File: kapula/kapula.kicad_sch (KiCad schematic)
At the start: 160 parts, among them J1 Conn_02x10_Odd_Even, J12 U.FL, J13 U.FL, J3 U.FL, J4 Conn_ARM_JTAG_SWD_10, J5 U.FL, J9 U.FL, Q1 AO3401A, Q1 BSS84, Q2 AO3401A, Q3 AO3400A, Q5 AO3400A, Q6 AO3400A, T1 BW21S7511A01TF, T2 BW21S7511A01TF, T3 BW21S7511A01TF, T4 BW21S7511A01TF, U1 XC6206P332MR, U2 TP4054, U3 DW01+G, U5 EFR32FG14P233F256GM48-B, U6 XA213-G4J, X1 DSB221SDN, Y1 32768 Hz

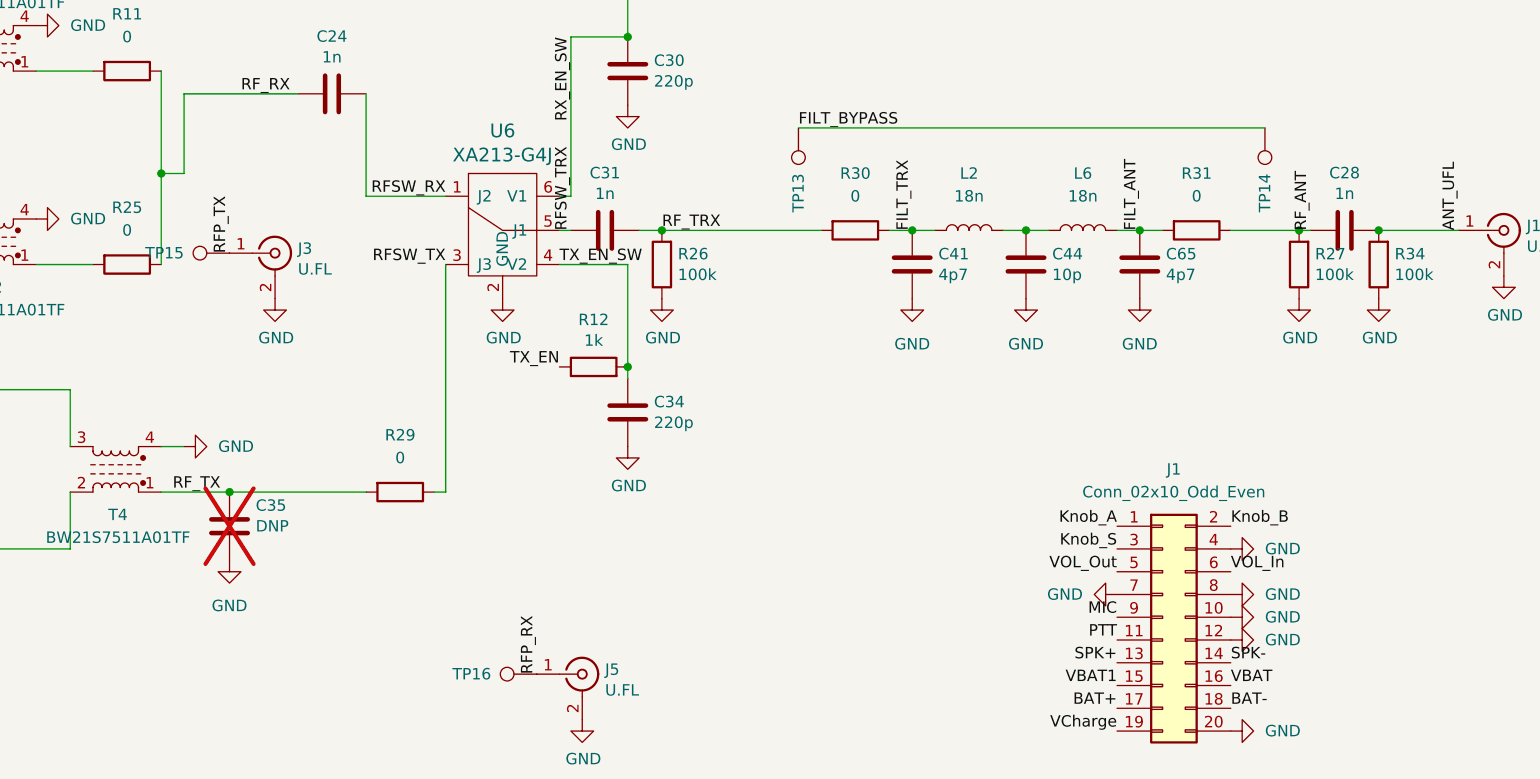
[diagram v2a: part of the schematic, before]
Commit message: Length match balanced TX line
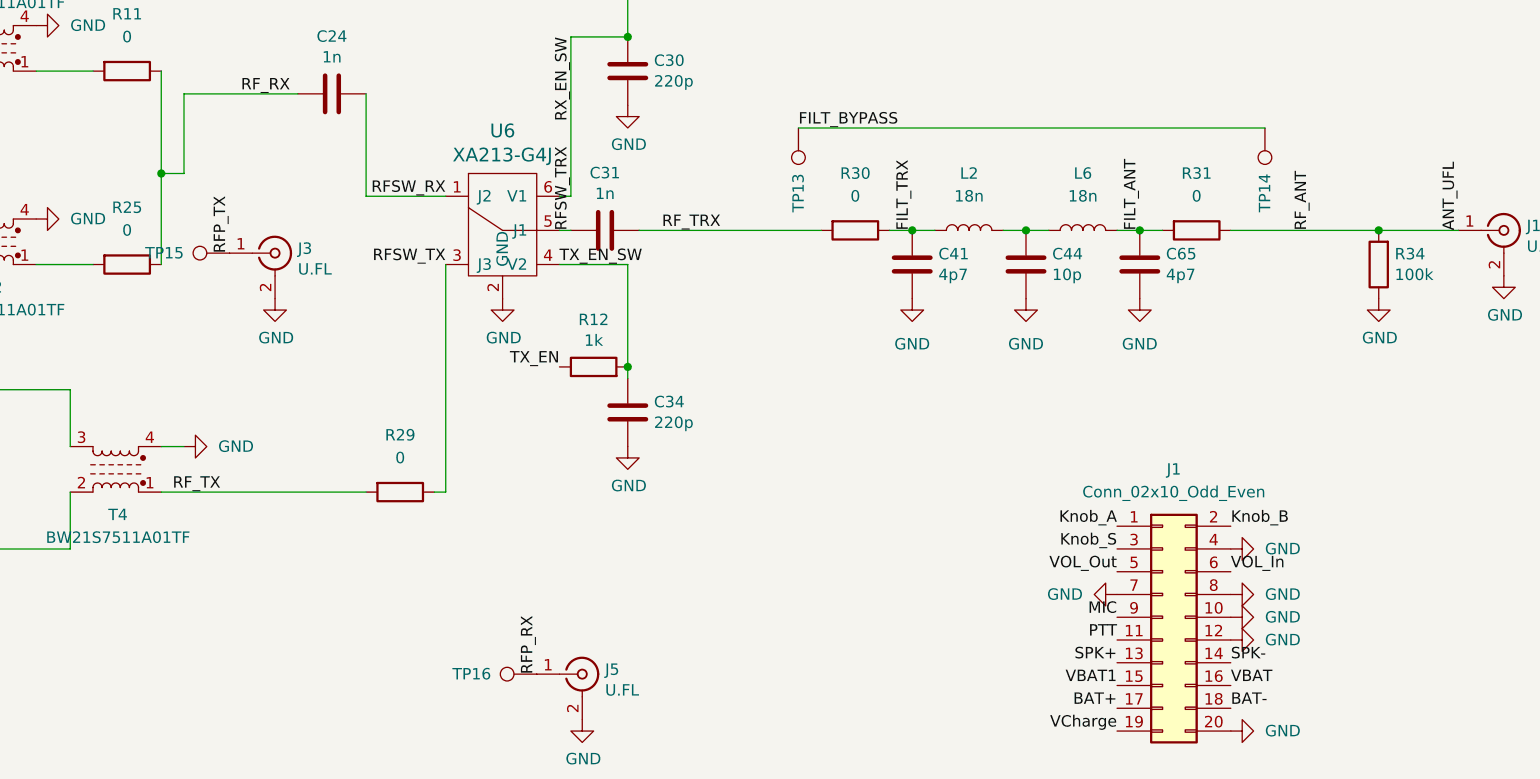
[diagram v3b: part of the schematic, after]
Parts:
- removed C28: 1n, Capacitor_SMD:C_0402_1005Metric, symbol Device:C
- removed C35: DNP, kapula:C_0402_to_0603_HandSolder, symbol Device:C
- removed R26, R27: 100k, Resistor_SMD:R_0402_1005Metric, symbol Device:R
- L10, L7: footprint Inductor_SMD:L_0402_1005Metric -> kapula:L_0402_to_0603_HandSolder
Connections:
- net RF_ANT is gone; now on net ANT_UFL: R31.1
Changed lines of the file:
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@@
   (junction (at 214.63 26.67) (diameter 0) (color 0 0 0 0)
   )
-  (junction (at 391.16 142.24) (diameter 0) (color 0 0 0 0)
-  )
   (junction (at 350.52 57.15) (diameter 0) (color 0 0 0 0)
   )
@@
   (junction (at 171.45 46.99) (diameter 0) (color 0 0 0 0)
   )
-  (junction (at 311.15 142.24) (diameter 0) (color 0 0 0 0)
-  )
   (junction (at 82.55 203.2) (diameter 0) (color 0 0 0 0)
   )
@@
   (junction (at 157.48 39.37) (diameter 0) (color 0 0 0 0)
   )
-  (junction (at 382.27 142.24) (diameter 0) (color 0 0 0 0)
-  )
   (junction (at 173.99 189.23) (diameter 0) (color 0 0 0 0)
   )
@@
   (junction (at 231.14 132.08) (diameter 0) (color 0 0 0 0)
   )
+  (junction (at 391.16 142.24) (diameter 0) (color 0 0 0 0)
+  )
   (junction (at 185.42 137.16) (diameter 0) (color 0 0 0 0)
   )
@@
   (junction (at 156.21 82.55) (diameter 0) (color 0 0 0 0)
   )
-  (junction (at 262.89 171.45) (diameter 0) (color 0 0 0 0)
-  )
   (junction (at 66.04 26.67) (diameter 0) (color 0 0 0 0)
   )
@@
     (stroke (width 0) (type default))
   )
-  (wire (pts (xy 311.15 142.24) (xy 328.93 142.24))
-    (stroke (width 0) (type default))
-  )
-  (wire (pts (xy 262.89 171.45) (xy 278.13 171.45))
+  (wire (pts (xy 308.61 142.24) (xy 328.93 142.24))
     (stroke (width 0) (type default))
   )
@@
     (stroke (width 0) (type default))
   )
-  (wire (pts (xy 382.27 142.24) (xy 383.54 142.24))
+  (wire (pts (xy 374.65 142.24) (xy 391.16 142.24))
     (stroke (width 0) (type default))
   )
@@
     (stroke (width 0) (type default))
   )
-  (wire (pts (xy 374.65 142.24) (xy 382.27 142.24))
-    (stroke (width 0) (type default))
-  )
   (wire (pts (xy 220.98 119.38) (xy 231.14 119.38))
     (stroke (width 0) (type default))
@@
     (stroke (width 0) (type default))
   )
-  (wire (pts (xy 308.61 142.24) (xy 311.15 142.24))
-    (stroke (width 0) (type default))
-  )
   (wire (pts (xy 176.53 85.09) (xy 176.53 124.46))
     (stroke (width 0) (type default))
@@
     (stroke (width 0) (type default))
   )
-  (wire (pts (xy 262.89 171.45) (xy 255.27 171.45))
+  (wire (pts (xy 255.27 171.45) (xy 278.13 171.45))
     (stroke (width 0) (type default))
   )
@@
     )
   )
-  (symbol (lib_id "Device:R") (at 311.15 146.05 180) (unit 1)
-    (in_bom yes) (on_board yes) (dnp no)
-    (property "Reference" "R26" (at 312.928 144.8816 0)
-      (effects (font (size 1.27 1.27)) (justify right))
-    )
-    (property "Value" "100k" (at 312.928 147.193 0)
-      (effects (font (size 1.27 1.27)) (justify right))
-    )
-    (property "Footprint" "Resistor_SMD:R_0402_1005Metric" (at 312.928 146.05 90)
-      (effects (font (size 1.27 1.27)) hide)
-    )
-    (property "Datasheet" "" (at 311.15 146.05 0)
-      (effects (font (size 1.27 1.27)) hide)
-    )
-    (property "LCSC" "" (at 311.15 146.05 0)
-      (effects (font (size 1.27 1.27)) hide)
-    )
-    (pin "1")
-    (pin "2")
-    (instances
-      (project "kapula"
-        (path "/f2315993-072e-45c9-8c85-e79c6d40aba4"
-          (reference "R26") (unit 1)
-        )
-      )
-    )
-  )
   (symbol (lib_id "power:GND") (at 241.3 140.97 90) (unit 1)
     (in_bom yes) (on_board yes) (dnp no) (fields_autoplaced)
@@
     )
   )
-  (symbol (lib_id "Device:R") (at 382.27 146.05 180) (unit 1)
-    (in_bom yes) (on_board yes) (dnp no)
-    (property "Reference" "R27" (at 384.048 144.8816 0)
-      (effects (font (size 1.27 1.27)) (justify right))
-    )
-    (property "Value" "100k" (at 384.048 147.193 0)
-      (effects (font (size 1.27 1.27)) (justify right))
-    )
-    (property "Footprint" "Resistor_SMD:R_0402_1005Metric" (at 384.048 146.05 90)
-      (effects (font (size 1.27 1.27)) hide)
-    )
-    (property "Datasheet" "" (at 382.27 146.05 0)
-      (effects (font (size 1.27 1.27)) hide)
-    )
-    (property "LCSC" "" (at 382.27 146.05 0)
-      (effects (font (size 1.27 1.27)) hide)
-    )
-    (pin "1")
-    (pin "2")
-    (instances
-      (project "kapula"
-        (path "/f2315993-072e-45c9-8c85-e79c6d40aba4"
-          (reference "R27") (unit 1)
-        )
-      )
-    )
-  )
   (symbol (lib_id "Device:C") (at 215.9 265.43 0) (unit 1)
     (in_bom yes) (on_board yes) (dnp no)
@@
     )
   )
-  (symbol (lib_id "Device:C") (at 262.89 175.26 0) (unit 1)
-    (in_bom no) (on_board yes) (dnp yes)
-    (property "Reference" "C35" (at 265.811 172.9486 0)
-      (effects (font (size 1.27 1.27)) (justify left))
-    )
-    (property "Value" "DNP" (at 265.811 175.26 0)
-      (effects (font (size 1.27 1.27)) (justify left))
-    )
-    (property "Footprint" "kapula:C_0402_to_0603_HandSolder" (at 263.8552 179.07 0)
-      (effects (font (size 1.27 1.27)) hide)
-    )
-    (property "Datasheet" "" (at 262.89 175.26 0)
-      (effects (font (size 1.27 1.27)) hide)
-    )
-    (pin "1")
-    (pin "2")
-    (instances
-      (project "kapula"
-        (path "/f2315993-072e-45c9-8c85-e79c6d40aba4"
-          (reference "C35") (unit 1)
-        )
-      )
-    )
-  )
   (symbol (lib_id "Transistor_FET:BSS84") (at 386.08 -19.05 270) (mirror x) (unit 1)
     (in_bom yes) (on_board yes) (dnp no)
@@
     )
   )
-  (symbol (lib_id "power:GND") (at 262.89 179.07 0) (unit 1)
-    (in_bom yes) (on_board yes) (dnp no) (fields_autoplaced)
-    (property "Reference" "#PWR0112" (at 262.89 185.42 0)
-      (effects (font (size 1.27 1.27)) hide)
-    )
-    (property "Value" "GND" (at 262.89 184.15 0)
-      (effects (font (size 1.27 1.27)))
-    )
-    (property "Footprint" "" (at 262.89 179.07 0)
-      (effects (font (size 1.27 1.27)) hide)
-    )
-    (property "Datasheet" "" (at 262.89 179.07 0)
-      (effects (font (size 1.27 1.27)) hide)
-    )
-    (pin "1")
-    (instances
-      (project "kapula"
-        (path "/f2315993-072e-45c9-8c85-e79c6d40aba4"
-          (reference "#PWR0112") (unit 1)
-        )
-      )
-    )
-  )
   (symbol (lib_id "power:GND") (at 373.38 218.44 0) (unit 1)
     (in_bom yes) (on_board yes) (dnp no)
@@
       (effects (font (size 1.27 1.27)))
     )
-    (property "Footprint" "Inductor_SMD:L_0402_1005Metric" (at 195.58 177.8 0)
+    (property "Footprint" "kapula:L_0402_to_0603_HandSolder" (at 195.58 177.8 0)
       (effects (font (size 1.27 1.27)) hide)
     )
@@
     )
   )
-  (symbol (lib_id "power:GND") (at 382.27 149.86 0) (unit 1)
-    (in_bom yes) (on_board yes) (dnp no)
-    (property "Reference" "#PWR0110" (at 382.27 156.21 0)
-      (effects (font (size 1.27 1.27)) hide)
-    )
-    (property "Value" "GND" (at 382.397 154.2542 0)
-      (effects (font (size 1.27 1.27)))
-    )
-    (property "Footprint" "" (at 382.27 149.86 0)
-      (effects (font (size 1.27 1.27)) hide)
-    )
-    (property "Datasheet" "" (at 382.27 149.86 0)
-      (effects (font (size 1.27 1.27)) hide)
-    )
-    (pin "1")
-    (instances
-      (project "kapula"
-        (path "/f2315993-072e-45c9-8c85-e79c6d40aba4"
-          (reference "#PWR0110") (unit 1)
-        )
-      )
-    )
-  )
   (symbol (lib_id "Device:R") (at 377.19 -17.78 180) (unit 1)
     (in_bom yes) (on_board yes) (dnp no)
@@
     )
   )
-  (symbol (lib_id "Device:C") (at 387.35 142.24 270) (unit 1)
-    (in_bom yes) (on_board yes) (dnp no)
-    (property "Reference" "C28" (at 387.35 135.8392 90)
-      (effects (font (size 1.27 1.27)))
-    )
-    (property "Value" "1n" (at 387.35 138.1506 90)
-      (effects (font (size 1.27 1.27)))
-    )
-    (property "Footprint" "Capacitor_SMD:C_0402_1005Metric" (at 383.54 143.2052 0)
-      (effects (font (size 1.27 1.27)) hide)
-    )
-    (property "Datasheet" "" (at 387.35 142.24 0)
-      (effects (font (size 1.27 1.27)) hide)
-    )
-    (property "LCSC" "C1523" (at 387.35 142.24 0)
-      (effects (font (size 1.27 1.27)) hide)
-    )
-    (pin "1")
-    (pin "2")
-    (instances
-      (project "kapula"
-        (path "/f2315993-072e-45c9-8c85-e79c6d40aba4"
-          (reference "C28") (unit 1)
-        )
-      )
-    )
-  )
   (symbol (lib_id "power:PWR_FLAG") (at 43.18 138.43 0) (unit 1)
     (in_bom yes) (on_board yes) (dnp no) (fields_autoplaced)
@@
       (effects (font (size 1.27 1.27)))
     )
-    (property "Footprint" "Inductor_SMD:L_0402_1005Metric" (at 195.58 160.02 0)
+    (property "Footprint" "kapula:L_0402_to_0603_HandSolder" (at 195.58 160.02 0)
       (effects (font (size 1.27 1.27)) hide)
     )
@@
         )
       )
-    )
-  )
-  (symbol (lib_id "power:GND") (at 311.15 149.86 0) (unit 1)
-    (in_bom yes) (on_board yes) (dnp no)
-    (property "Reference" "#PWR0107" (at 311.15 156.21 0)
-      (effects (font (size 1.27 1.27)) hide)
-    )
-    (property "Value" "GND" (at 311.277 154.2542 0)
-      (effects (font (size 1.27 1.27)))
-    )
-    (property "Footprint" "" (at 311.15 149.86 0)
-      (effects (font (size 1.27 1.27)) hide)
-    )
-    (property "Datasheet" "" (at 311.15 149.86 0)
-      (effects (font (size 1.27 1.27)) hide)
-    )
-    (pin "1")
-    (instances
-      (project "kapula"
-        (path "/f2315993-072e-45c9-8c85-e79c6d40aba4"
-          (reference "#PWR0107") (unit 1)
-        )
-      )

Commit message: Roughly place some power supply related components in layout
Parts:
- Q1, Q3, Q5, Q6: footprint Package_TO_SOT_SMD:SOT-23_Handsoldering -> Package_TO_SOT_SMD:SOT-23
- R2: footprint kapula:R_0402_to_0603_HandSolder -> Resistor_SMD:R_0402_1005Metric; LCSC C23179 -> C25117
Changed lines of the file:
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@@
       (effects (font (size 1.27 1.27)))
     )
-    (property "Footprint" "kapula:R_0402_to_0603_HandSolder" (at 166.37 41.148 90)
+    (property "Footprint" "Resistor_SMD:R_0402_1005Metric" (at 166.37 41.148 90)
       (effects (font (size 1.27 1.27)) hide)
     )
@@
       (effects (font (size 1.27 1.27)) hide)
     )
-    (property "LCSC" "C23179" (at 166.37 39.37 0)
+    (property "LCSC" "C25117" (at 166.37 39.37 0)
       (effects (font (size 1.27 1.27)) hide)
     )
@@
       (effects (font (size 1.27 1.27)))
     )
-    (property "Footprint" "Package_TO_SOT_SMD:SOT-23_Handsoldering" (at 80.645 24.13 0)
+    (property "Footprint" "Package_TO_SOT_SMD:SOT-23" (at 80.645 24.13 0)
       (effects (font (size 1.27 1.27) italic) (justify left) hide)
     )
@@
       (effects (font (size 1.27 1.27)))
     )
-    (property "Footprint" "Package_TO_SOT_SMD:SOT-23_Handsoldering" (at 197.485 63.5 0)
+    (property "Footprint" "Package_TO_SOT_SMD:SOT-23" (at 197.485 63.5 0)
       (effects (font (size 1.27 1.27) italic) (justify left) hide)
     )
@@
       (effects (font (size 1.27 1.27)))
     )
-    (property "Footprint" "Package_TO_SOT_SMD:SOT-23_Handsoldering" (at 180.975 63.5 0)
+    (property "Footprint" "Package_TO_SOT_SMD:SOT-23" (at 180.975 63.5 0)
       (effects (font (size 1.27 1.27) italic) (justify left) hide)
     )
@@
       (effects (font (size 1.27 1.27)))
     )
-    (property "Footprint" "Package_TO_SOT_SMD:SOT-23_Handsoldering" (at 200.66 -36.195 0)
+    (property "Footprint" "Package_TO_SOT_SMD:SOT-23" (at 200.66 -36.195 0)
       (effects (font (size 1.27 1.27) italic) (justify left) hide)
     )

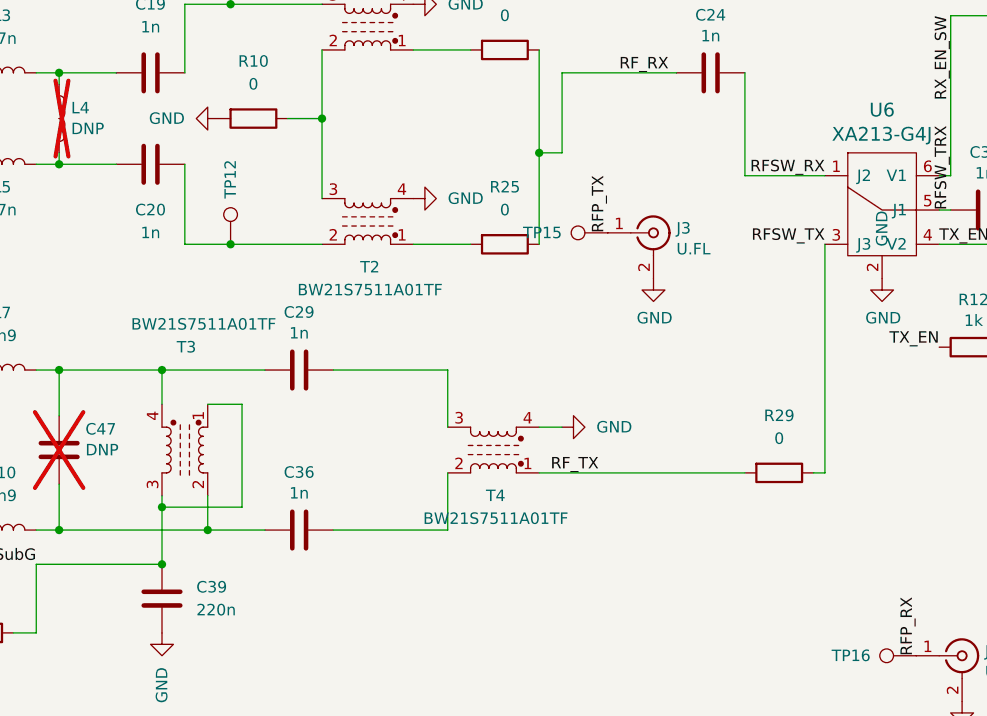
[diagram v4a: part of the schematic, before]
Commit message: PCB: Organize RF layout
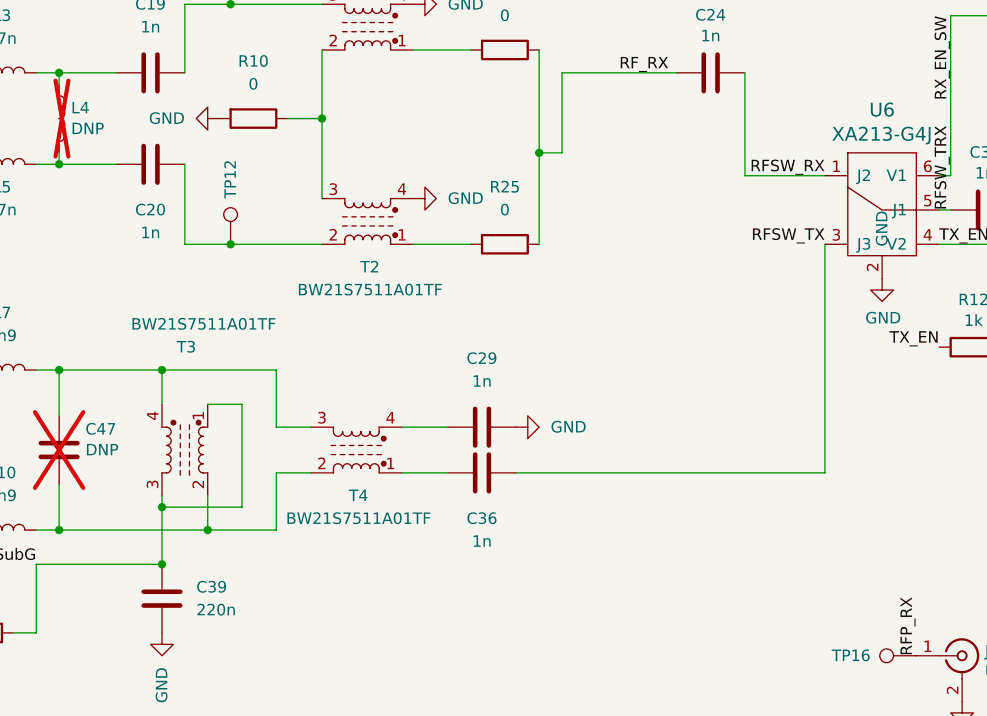
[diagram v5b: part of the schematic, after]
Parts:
- removed J3: U.FL, Connector_Coaxial:U.FL_Hirose_U.FL-R-SMT-1_Vertical, symbol Connector:Conn_Coaxial
- removed R29: 0, kapula:R_0402_to_0603_HandSolder, symbol Device:R
- removed TP15: ~, kapula:Pad_0402_1005Metric, symbol Connector:TestPoint
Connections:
- net GND: now also C29.1; no longer T4.4
- net RFSW_TX: now also C36.1
- net at C47.1, L7.1, T3.4: now also T4.3; no longer C29.2
- net at C47.2, L10.1, T3.2: now also T4.2; no longer C36.2
- net RF_TX: no longer names the net of T4.1
- net RF_TX: now also C36.2
- new net: C29.2, T4.4
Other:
- moved on the sheet: C29, C36, T4
